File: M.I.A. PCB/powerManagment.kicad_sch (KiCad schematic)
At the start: 42 parts, among them J2 Conn_01x02_Pin, U10 INA226, U11 AMS1117-3.3, U12 AP62150WU, U13 TPS2121RUXR, U14 AP62150WU, U9 TPS2121RUXR

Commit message: Worked on Layout, Changed IMU
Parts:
- added J14, J18: Screw_Terminal_01x02, TerminalBlock_Phoenix:TerminalBlock_Phoenix_MKDS-1-2-3.81_1x02_P3.81mm_Horizontal, symbol Connector:Screw_Terminal_01x02
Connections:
- net GND: now also J18.2 (Pin_2)
- net VSYS: now also J14.1 (Pin_1), J18.1 (Pin_1)
- new net V_IGN: J14.2 (Pin_2)
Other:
- note added: "V_OUT"
- note added: "arm switch"
- note added: "xt30"
- moved on the sheet: C27, C31, C32, C33, C35, C36, C37, J2, L2, L3, R16, R19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

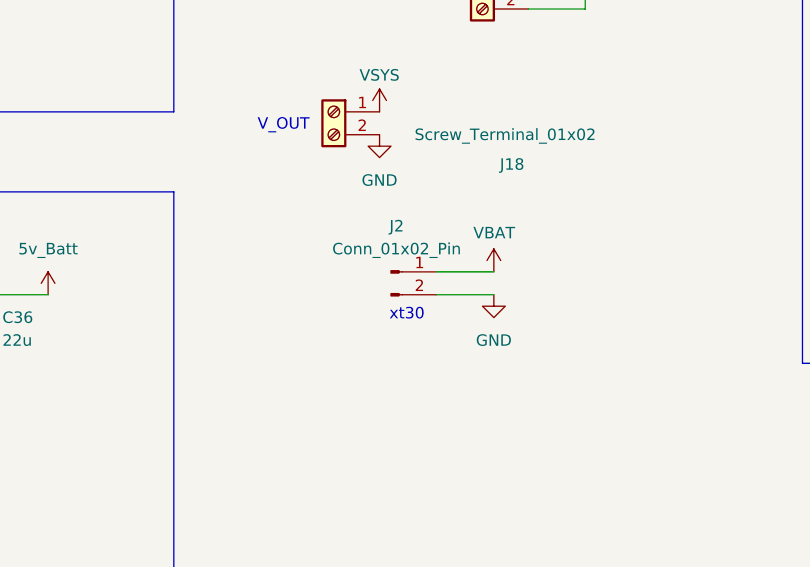
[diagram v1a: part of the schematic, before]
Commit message: added servo pin protector and changed screw terminal size
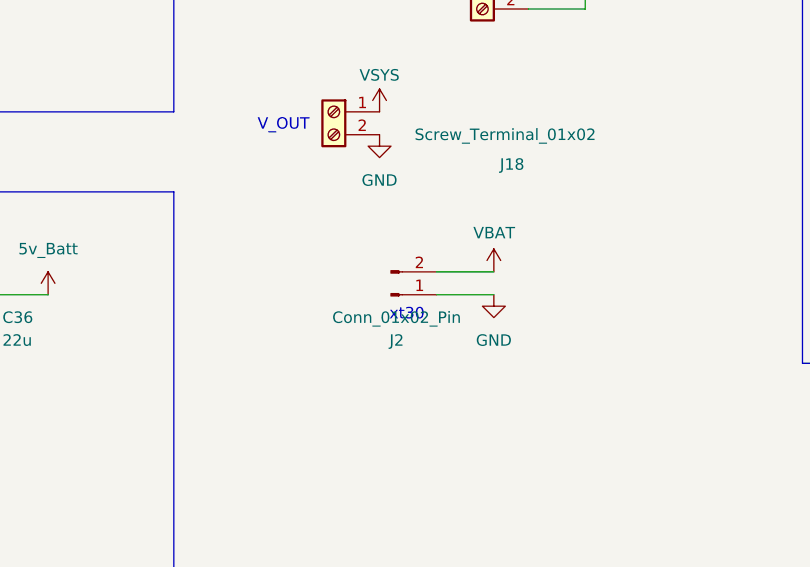
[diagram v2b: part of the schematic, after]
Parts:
- J14, J18: footprint TerminalBlock_Phoenix:TerminalBlock_Phoenix_MKDS-1-2-3.81_1x02_P3.81mm_Horizontal -> TerminalBlock_Phoenix:TerminalBlock_Phoenix_PT-1,5-2-3.5-H_1x02_P3.50mm_Horizontal
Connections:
- net GND: now also J2.1 (Pin_1); no longer J2.2 (Pin_2)
- net VBAT: now also J2.2 (Pin_2); no longer J2.1 (Pin_1)
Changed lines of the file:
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@@
 	(wire
 		(pts
+			(xy 146.05 149.86) (xy 152.4 149.86)
+		)
+		(stroke
+			(width 0)
+			(type default)
+		)
+	)
+	(wire
+		(pts
 			(xy 82.55 149.86) (xy 82.55 152.4)
 		)
@@
 	(wire
 		(pts
-			(xy 152.4 152.4) (xy 146.05 152.4)
-		)
-		(stroke
-			(width 0)
-			(type default)
-		)
-	)
-	(wire
-		(pts
 			(xy 59.69 68.58) (xy 59.69 67.31)
 		)
@@
 	(wire
 		(pts
-			(xy 146.05 149.86) (xy 152.4 149.86)
+			(xy 146.05 152.4) (xy 152.4 152.4)
 		)
 		(stroke
@@
 			)
 		)
-		(property "Footprint" "TerminalBlock_Phoenix:TerminalBlock_Phoenix_MKDS-1-2-3.81_1x02_P3.81mm_Horizontal"
+		(property "Footprint" "TerminalBlock_Phoenix:TerminalBlock_Phoenix_PT-1,5-2-3.5-H_1x02_P3.50mm_Horizontal"
 			(at 134.62 132.08 0)
 			(effects
@@
 	(symbol
 		(lib_id "Connector:Conn_01x02_Pin")
-		(at 140.97 149.86 0)
+		(at 140.97 152.4 0)
+		(mirror x)
 		(unit 1)
 		(exclude_from_sim no)
@@
 		(on_board yes)
 		(dnp no)
-		(fields_autoplaced yes)
 		(property "Reference" "J2"
-			(at 141.605 144.78 0)
+			(at 141.605 157.48 0)
 			(effects
 				(font
@@
 		)
 		(property "Value" "Conn_01x02_Pin"
-			(at 141.605 147.32 0)
+			(at 141.605 154.94 0)
 			(effects
 				(font
@@
 		)
 		(property "Footprint" "Connector_AMASS:AMASS_XT30PW-M_1x02_P2.50mm_Horizontal"
-			(at 140.97 149.86 0)
+			(at 140.97 152.4 0)
 			(effects
 				(font
@@
 		)
 		(property "Datasheet" "~"
-			(at 140.97 149.86 0)
+			(at 140.97 152.4 0)
 			(effects
 				(font
@@
 		)
 		(property "Description" "Generic connector, single row, 01x02, script generated"
-			(at 140.97 149.86 0)
+			(at 140.97 152.4 0)
 			(effects
 				(font
@@
 			)
 		)
-		(property "Footprint" "TerminalBlock_Phoenix:TerminalBlock_Phoenix_MKDS-1-2-3.81_1x02_P3.81mm_Horizontal"
+		(property "Footprint" "TerminalBlock_Phoenix:TerminalBlock_Phoenix_PT-1,5-2-3.5-H_1x02_P3.50mm_Horizontal"
 			(at 151.13 118.11 0)
 			(effects

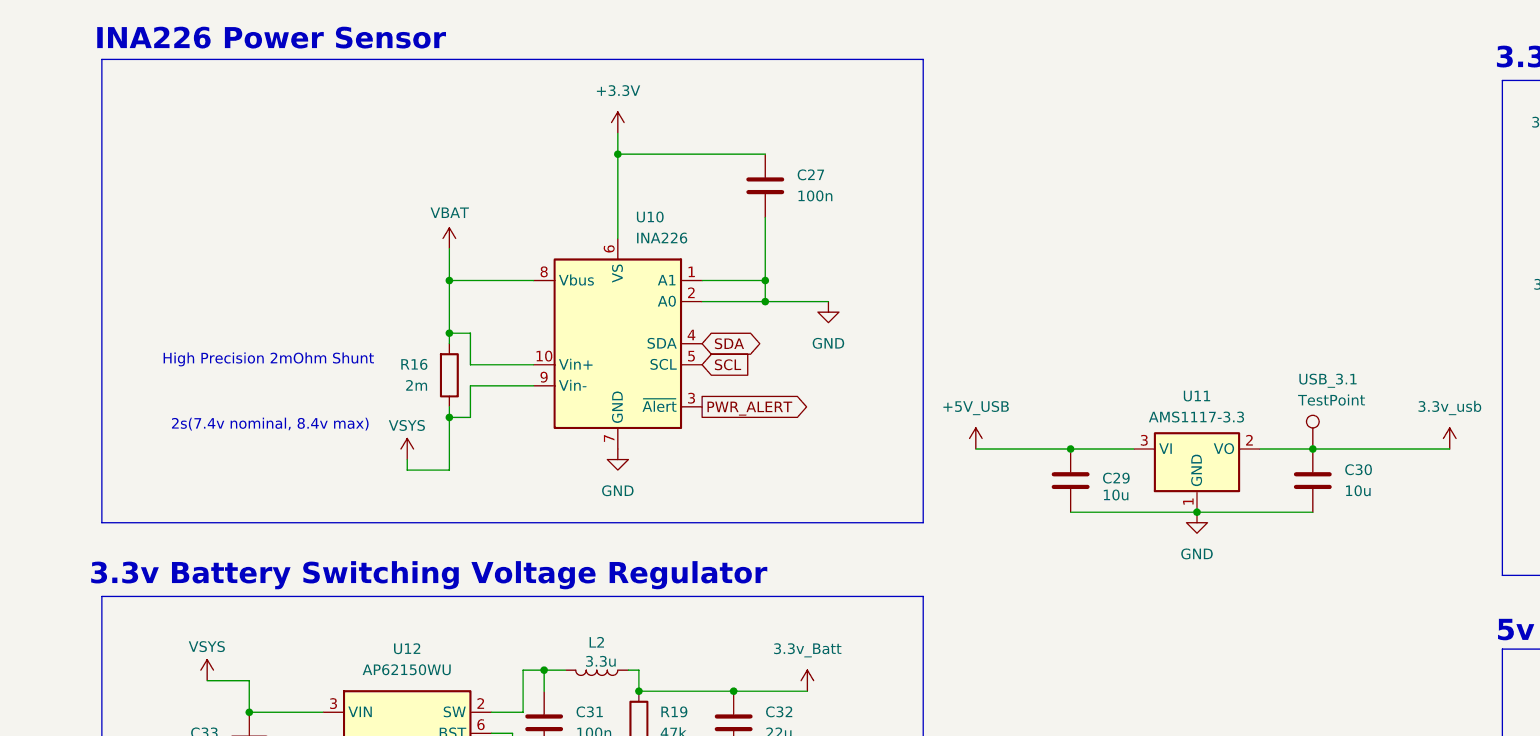
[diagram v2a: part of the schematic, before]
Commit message: updated LDO and Power Sensor
may need to change LDO to support power draw of RFM95CW
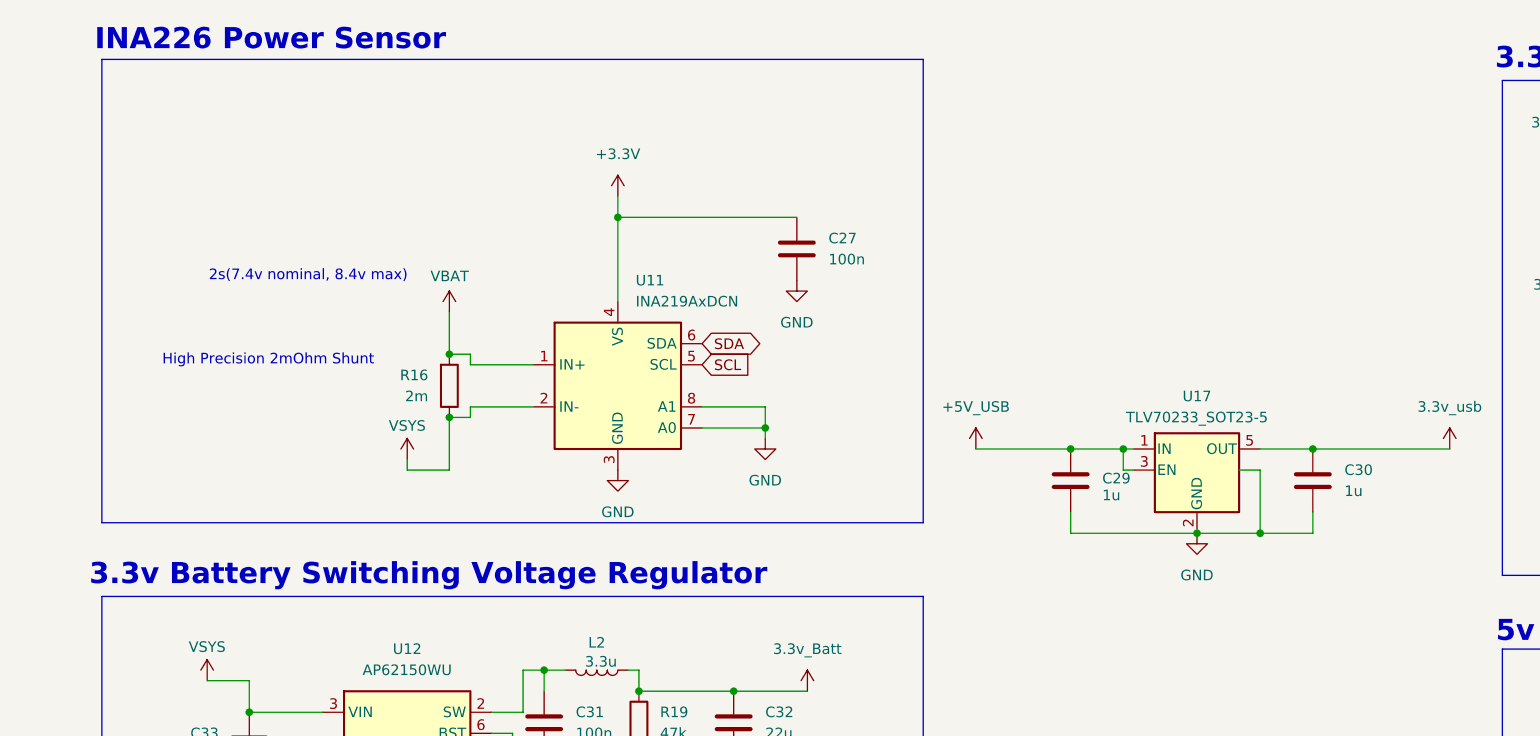
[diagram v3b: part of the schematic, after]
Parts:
- removed U10: INA226, Package_SO:VSSOP-10_3x3mm_P0.5mm, symbol Sensor_Energy:INA226
- removed U11: AMS1117-3.3, Package_TO_SOT_SMD:SOT-223-3_TabPin2, symbol Regulator_Linear:AMS1117-3.3
- removed USB_3.1: TestPoint, TestPoint:TestPoint_Pad_D1.0mm, symbol Connector:TestPoint
- added U11: INA219AxDCN, Package_TO_SOT_SMD:SOT-23-8, symbol Sensor_Energy:INA219AxDCN
- added U17: TLV70233_SOT23-5, Package_TO_SOT_SMD:SOT-23-5, symbol Regulator_Linear:TLV70233_SOT23-5
- C29, C30: value 10u -> 1u
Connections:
- net +3.3V: now also U11.4 (VS)
- net +5V_USB: now also U17.1 (IN), U17.3 (EN)
- net 3.3v_usb: now also U17.5 (OUT)
- net GND: now also U11.3 (GND), U11.7 (A0), U11.8 (A1), U17.2 (GND), U17.4 (NC)
- net SCL: now also U11.5 (SCL)
- net SDA: now also U11.6 (SDA)
- net VBAT: now also U11.1 (IN+)
- net VSYS: now also U11.2 (IN-)
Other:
- moved on the sheet: C27, R16

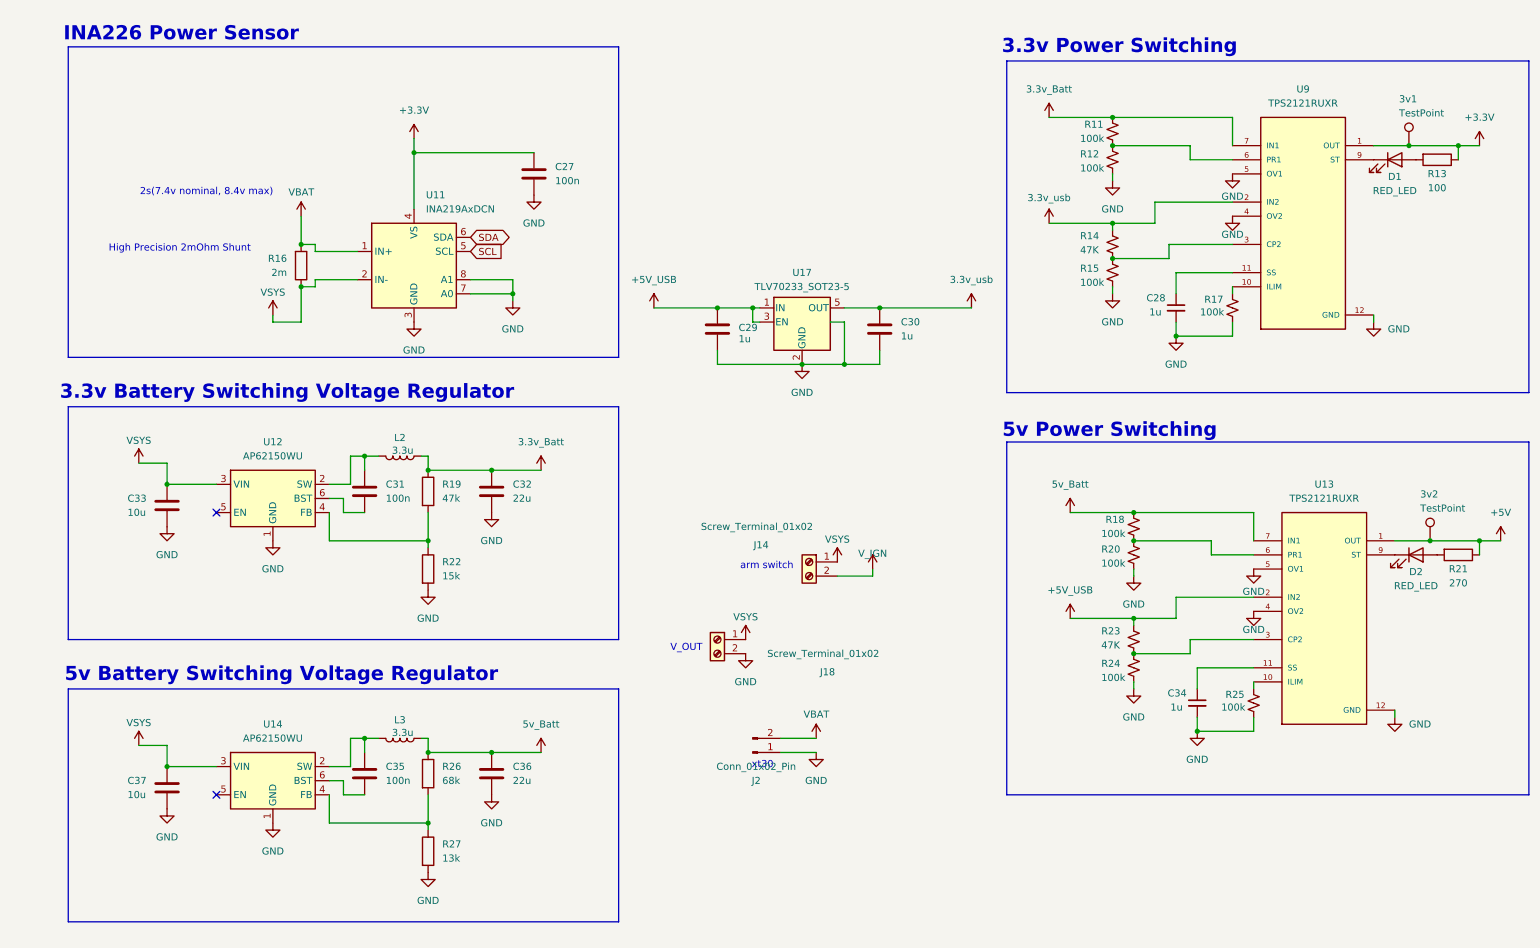
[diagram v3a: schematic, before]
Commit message: Finished Layout other than gps, extra connectors, and ignition lines
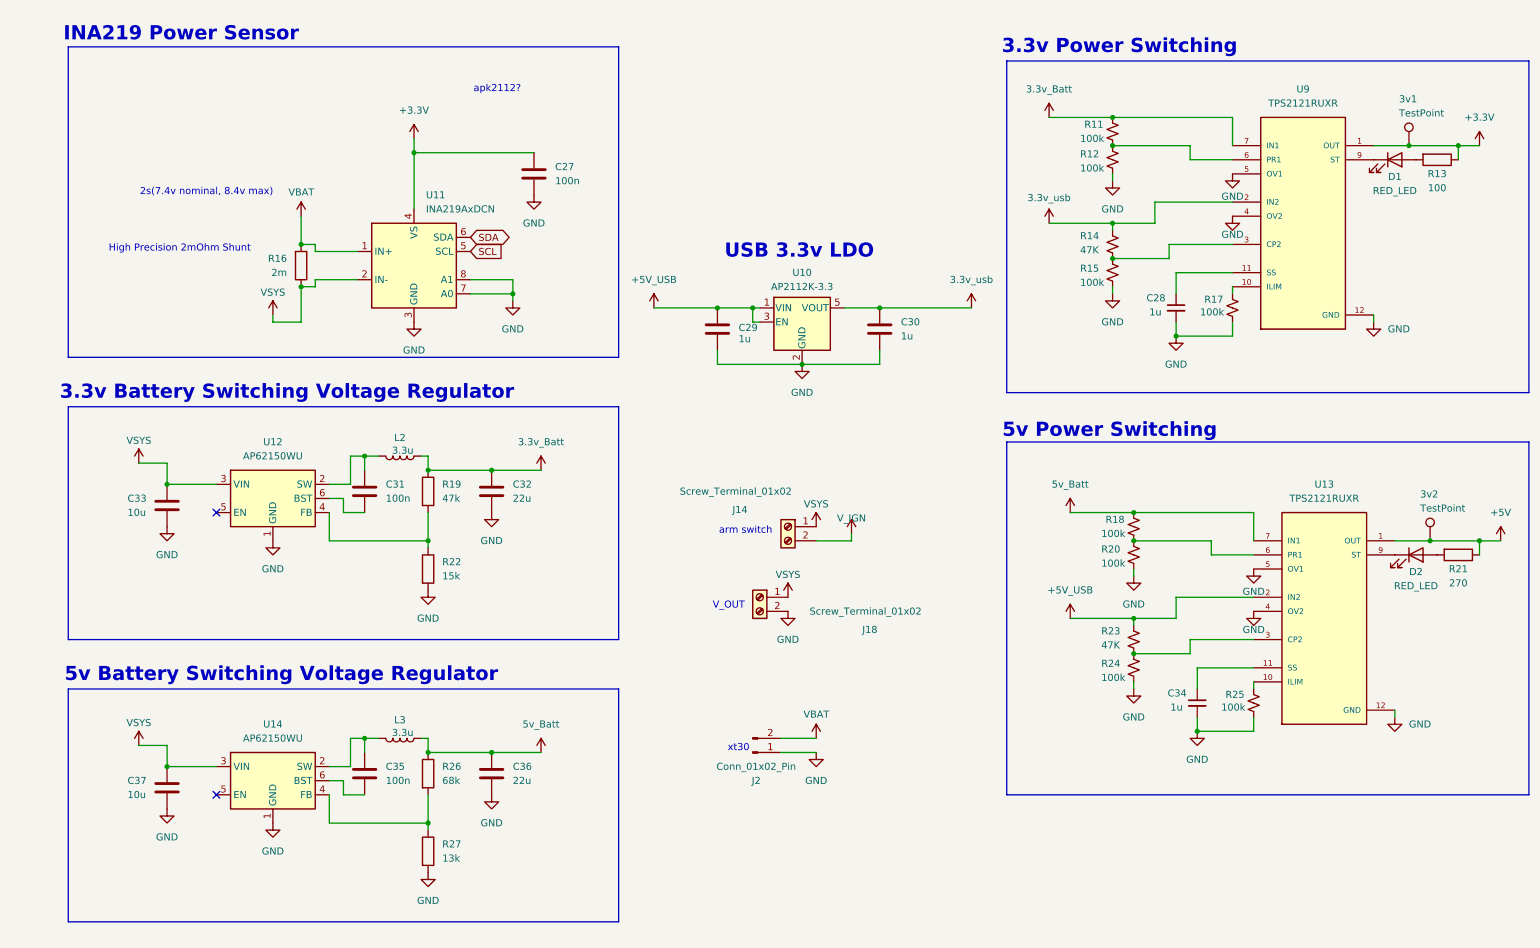
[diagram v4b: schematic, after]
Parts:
- removed U17: TLV70233_SOT23-5, Package_TO_SOT_SMD:SOT-23-5, symbol Regulator_Linear:TLV70233_SOT23-5
- added U10: AP2112K-3.3, Package_TO_SOT_SMD:SOT-23-5, symbol Regulator_Linear:AP2112K-3.3
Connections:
- net +5V_USB: now also U10.1 (VIN), U10.3 (EN)
- net 3.3v_usb: now also U10.5 (VOUT)
- net GND: now also U10.2 (GND)
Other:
- note added: "INA219 Power Sensor"
- note added: "USB 3.3v LDO"
- note added: "apk2112?"
- note removed: "INA226 Power Sensor"
- moved on the sheet: J14, J18

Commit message: Worked More on Layout/Wiring
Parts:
- J14, J18: footprint TerminalBlock_Phoenix:TerminalBlock_Phoenix_PT-1,5-2-3.5-H_1x02_P3.50mm_Horizontal -> PCM_SparkFun-Connector:ScrewTerminal_1x02_P3.5mm_Horizontal_Black
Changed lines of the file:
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@@
 			)
 		)
-		(property "Footprint" "TerminalBlock_Phoenix:TerminalBlock_Phoenix_PT-1,5-2-3.5-H_1x02_P3.50mm_Horizontal"
+		(property "Footprint" "PCM_SparkFun-Connector:ScrewTerminal_1x02_P3.5mm_Horizontal_Black"
 			(at 142.24 124.46 0)
 			(effects
@@
 			)
 		)
-		(property "Footprint" "TerminalBlock_Phoenix:TerminalBlock_Phoenix_PT-1,5-2-3.5-H_1x02_P3.50mm_Horizontal"
+		(property "Footprint" "PCM_SparkFun-Connector:ScrewTerminal_1x02_P3.5mm_Horizontal_Black"
 			(at 147.32 111.76 0)
 			(effects

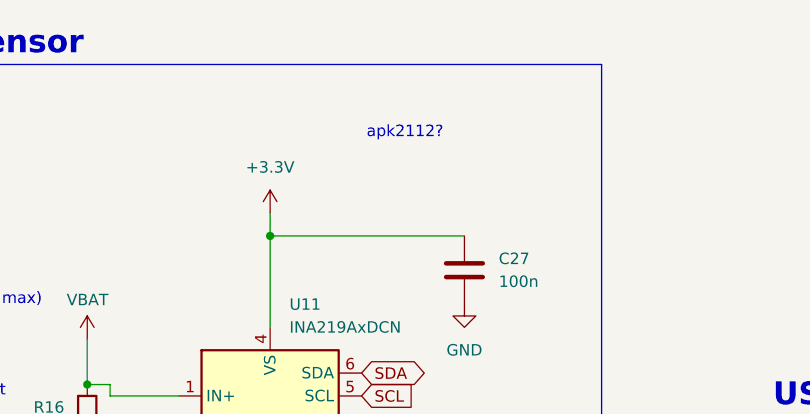
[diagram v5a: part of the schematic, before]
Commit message: Routed GPS Maybe Correctly
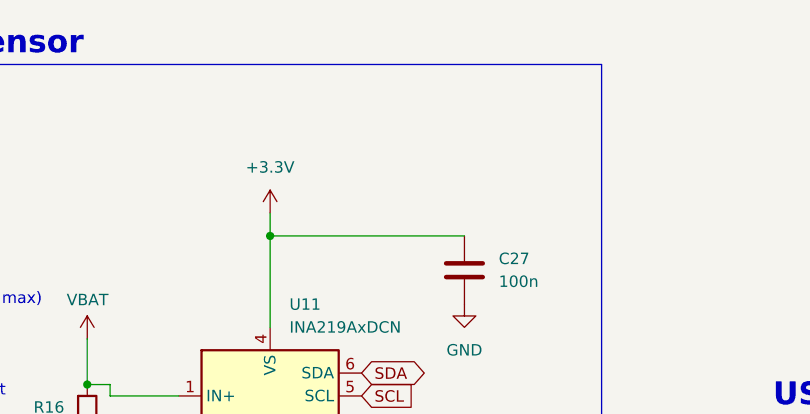
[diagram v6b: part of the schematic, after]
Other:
- note removed: "apk2112?"
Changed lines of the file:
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@@
-		)
-	)
-	(text "apk2112?"
-		(exclude_from_sim no)
-		(at 94.996 33.02 0)
-		(effects
-			(font
-				(size 1.27 1.27)
-			)
 		)
 	)
